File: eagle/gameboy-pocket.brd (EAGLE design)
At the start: 71.2 x 116.5 mm, 33 parts, among them J1 AUDIO_JACK_3.5MM_PTH, U1 LM4875

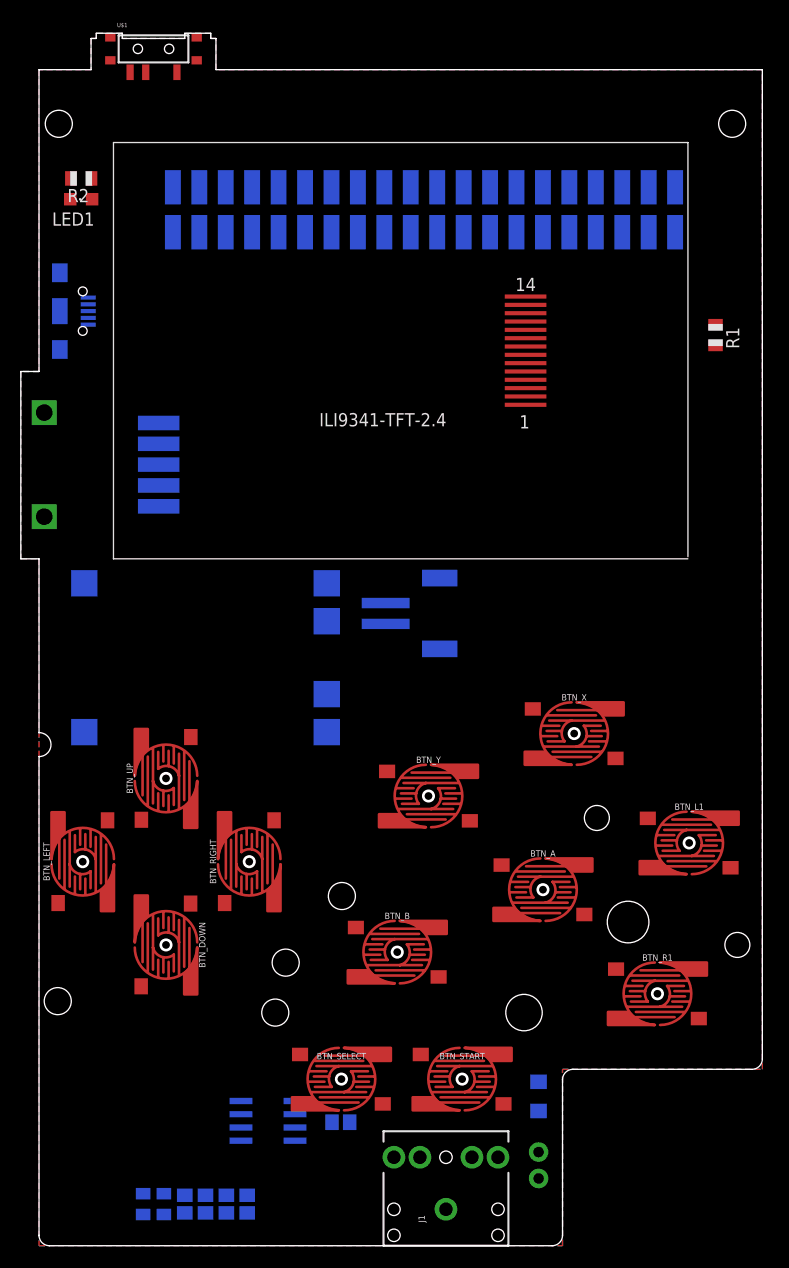
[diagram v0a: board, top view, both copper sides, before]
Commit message: all traces ripped up and placement accurate
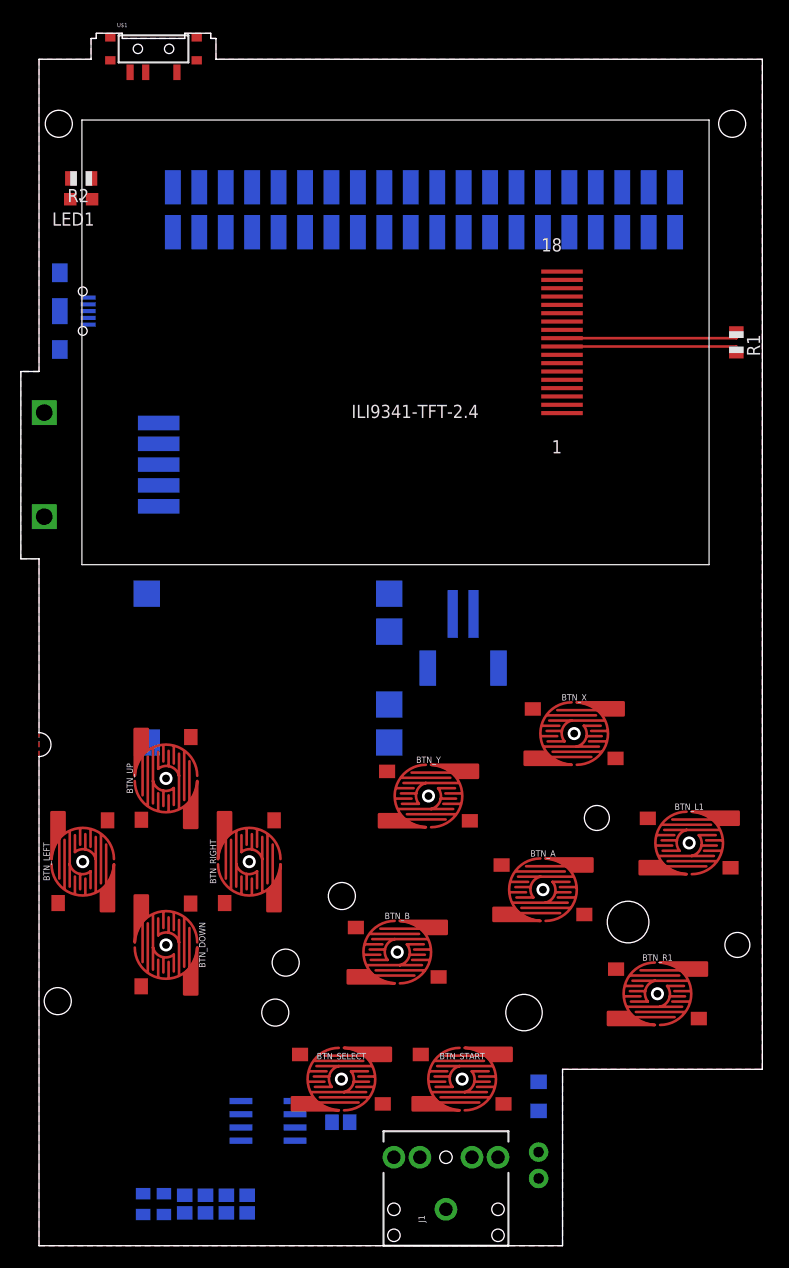
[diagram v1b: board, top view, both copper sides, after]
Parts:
- ILI9341-TFT-2.4: value GAMEBOYZEROHANDHELDDISPLAYS-2.2 -> GAMEBOYZEROHANDHELDDISPLAYS-2.4; device GameboyZeroHandheldDisplays:GAMEBOYZEROHANDHELDDISPLAYS-2.2 -> GameboyZeroHandheldDisplays:GAMEBOYZEROHANDHELDDISPLAYS-2.4
- moved POWER1 6.08 mm to (35.0, 64.0)
- moved J3 5.30 mm to (40.8, 57.0), turned to 180 degrees
- moved R1 2.12 mm to (67.0, 86.8)
- moved ILI9341-TFT-2.4 0.94 mm to (34.2, 86.8)
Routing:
- net 3V3: track 0.00 -> 17.4 mm
- net 3V3100OHM: track 0.00 -> 17.3 mm
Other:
- outline, holes or cut-outs redrawn

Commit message: routed main components and usb for charging
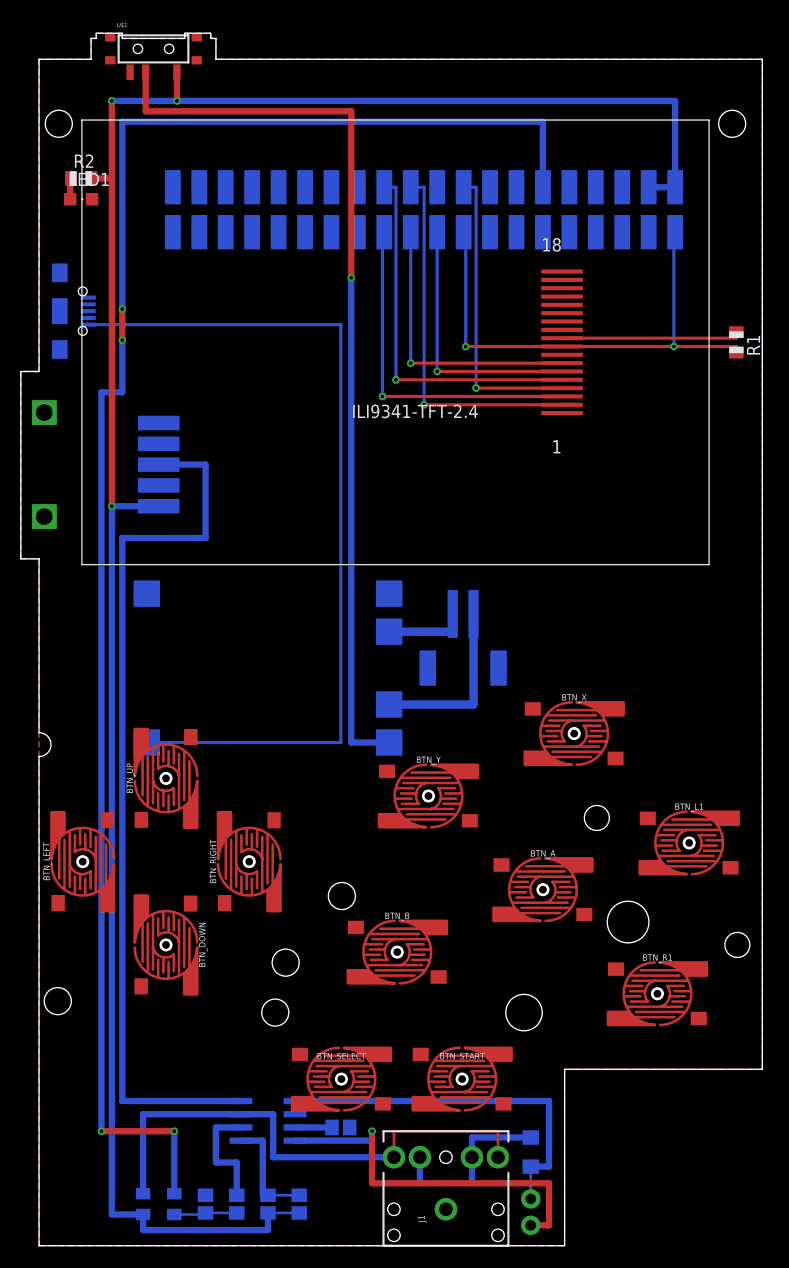
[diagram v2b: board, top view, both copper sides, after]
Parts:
- moved C2 5.40 mm to (47.2, 9.00), turned to 270 degrees
- moved C11 5.00 mm to (25.0, 4.00)
- moved J2 4.56 mm to (47.2, 4.50)
- moved C12 4.00 mm to (22.0, 4.00)
- moved C3 3.00 mm to (19.0, 4.00)
- moved C4 2.00 mm to (16.0, 4.00)
- moved R3 1.00 mm to (13.0, 4.00)
- moved C10 0.50 mm to (29.0, 11.4)
- turned LED1 to 270 degrees
- turned R2 to 0 degrees
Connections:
- net N$1 renamed VUSB
- net GND: now also POWER1.IN-
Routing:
- net SWITCH_OUT+: track 0.00 -> 202.3 mm, vias 0 -> 3
- net PWM: track 0.00 -> 158.7 mm, vias 0 -> 4
- net SWITCH_IN+: track 0.00 -> 87.8 mm, vias 0 -> 1
- net DC_VOL: track 0.00 -> 85.0 mm
- net VUSB: track 0.00 -> 83.1 mm
- net HEADPHONES: track 0.00 -> 50.9 mm
- net VOUT2: track 0.00 -> 36.1 mm, vias 0 -> 1
- net CSX: track 0.00 -> 35.6 mm, vias 0 -> 1
- net VOUT1: track 0.00 -> 35.6 mm
- net RESET: track 0.00 -> 35.4 mm, vias 0 -> 1
- net SCL: track 0.00 -> 33.2 mm, vias 0 -> 1
- net 3V3: track 17.4 -> 48.9 mm, vias 0 -> 2
- net D/CX: track 0.00 -> 28.8 mm, vias 0 -> 1
- net SDO: track 0.00 -> 27.1 mm, vias 0 -> 1
- net SDI: track 0.00 -> 25.4 mm, vias 0 -> 1
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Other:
- outline, holes or cut-outs redrawn
